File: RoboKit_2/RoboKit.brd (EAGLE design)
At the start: 134 x 82 mm, 28 parts, among them P1 B6B-PH-K, P2 B6B-PH-K, U1 CD74HC4067SM96, X1 JST-XH-03-PIN-LONG-PAD, X2 JST-XH-02-PIN-LONG-PAD, X3 JST-XH-02-PIN-LONG-PAD, X4 JST-XH-02-PIN-LONG-PAD, X5 JST-XH-04-PIN-LONG-PAD, X6 JST-XH-04-PIN-LONG-PAD, X7 JST-XH-10-PIN-LONG-PAD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

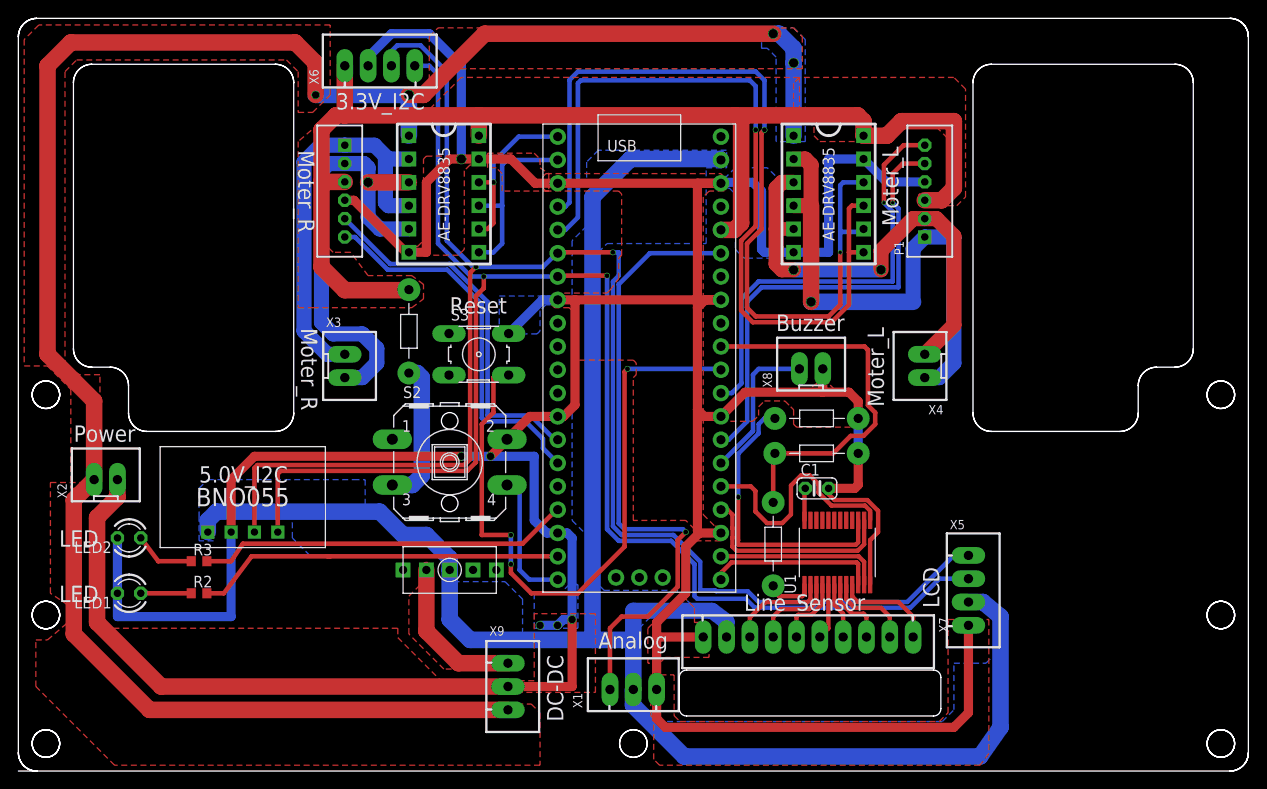
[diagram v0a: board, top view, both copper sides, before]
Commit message: マルチプレクサの電源回り付近を修正
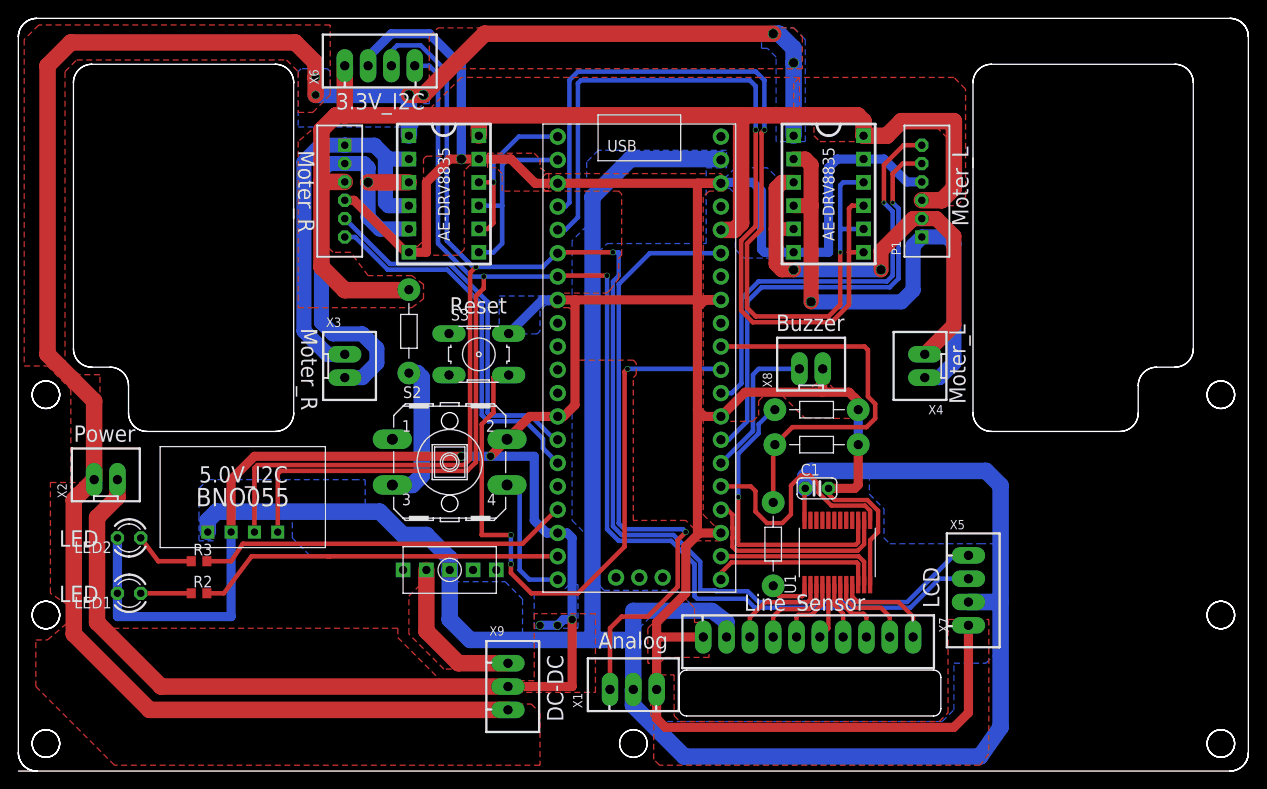
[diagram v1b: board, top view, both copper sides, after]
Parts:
- moved CONNECTOR5 0.95 mm to (87.0, 35.6)
- moved CONNECTOR6 0.95 mm to (87.0, 39.4)
- moved P1 0.32 mm to (98.4, 63.2)
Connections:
- removed net $10: C1.1, U1.24
- net VSYS: now also C1.1, U1.24
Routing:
- net VSYS: track 204.5 -> 245.2 mm
- net $10: track 3.51 -> 0.00 mm
- net MOTOR_A_R: track 58.4 -> 57.5 mm
- net GND: track 505.7 -> 504.8 mm
- net HALL_A_R: track 50.5 -> 49.6 mm
- net HALL_B_R: track 47.6 -> 46.9 mm
- net VOUT: vias 4 -> 6
